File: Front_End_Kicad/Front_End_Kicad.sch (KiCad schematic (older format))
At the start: 41 parts, among them J101 Barrel_Jack, SW101 SW_DIP_x02, SW102 SW_DIP_x02, SW103 SW_DIP_x05, SW104 SW_DIP_x05, U101 LMH6551MM

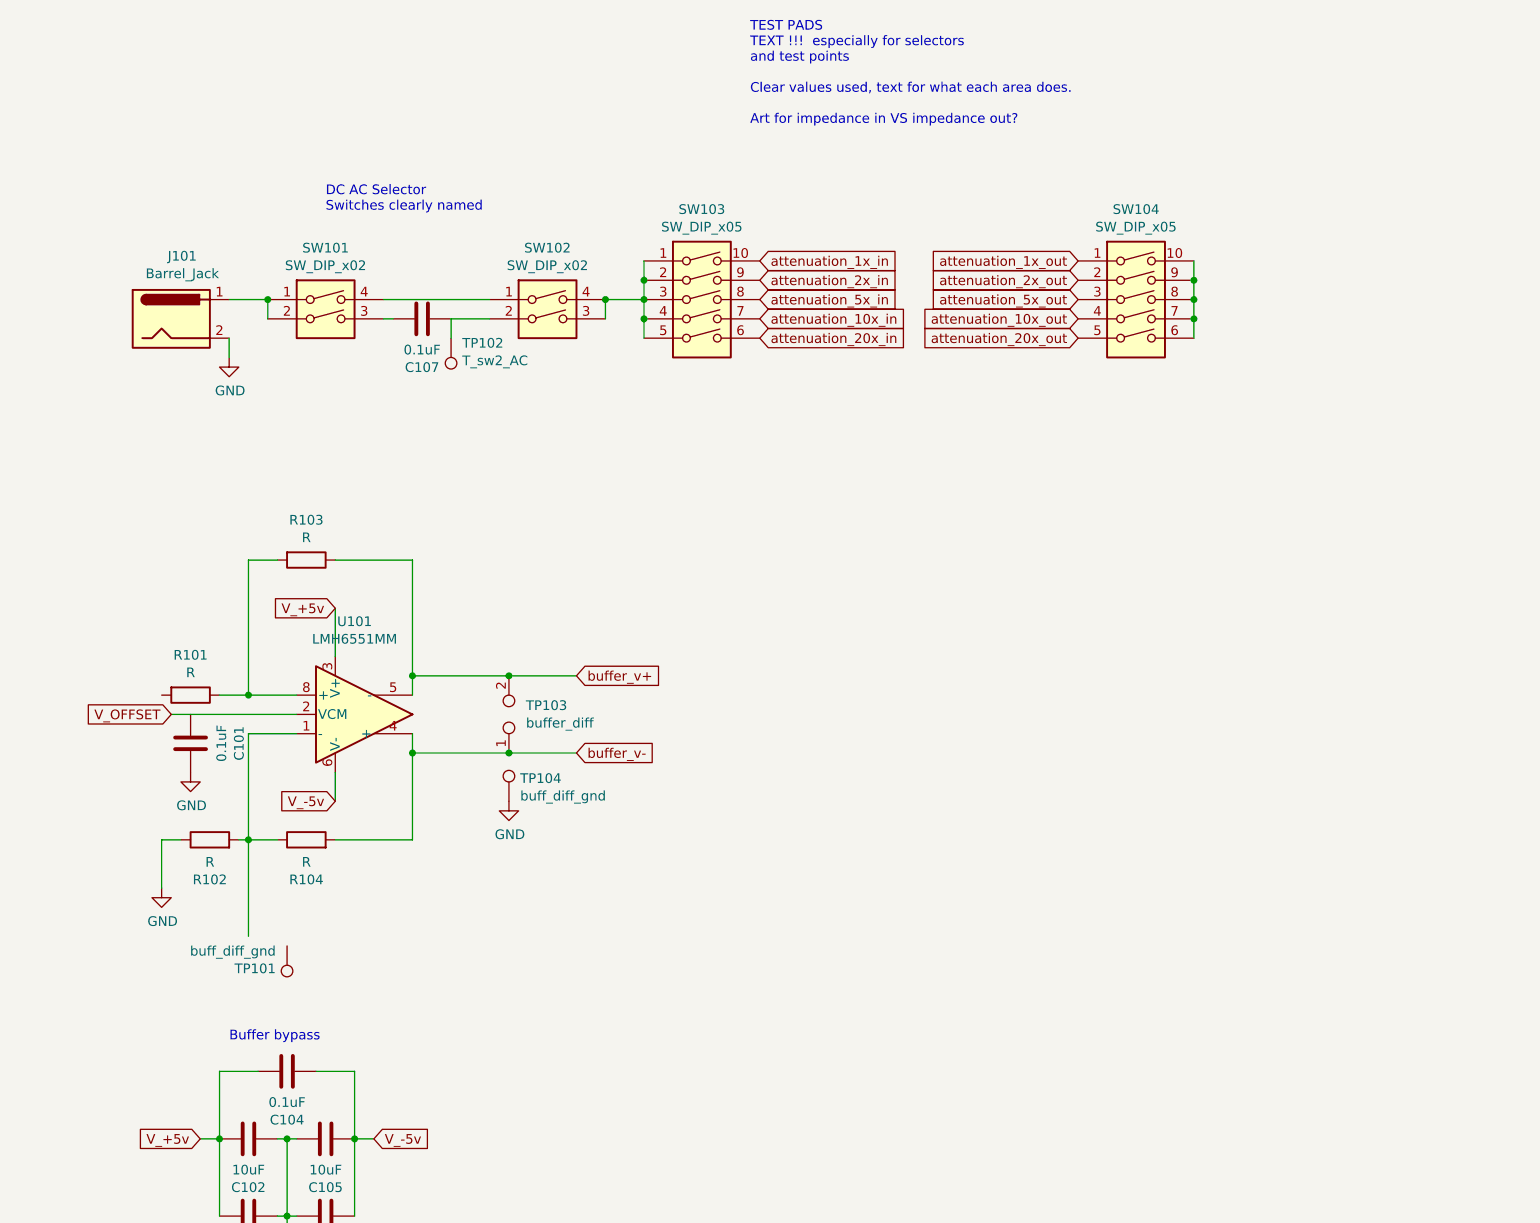
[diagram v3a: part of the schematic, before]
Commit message: All parts designed in schematic and preparing to enter PCB design
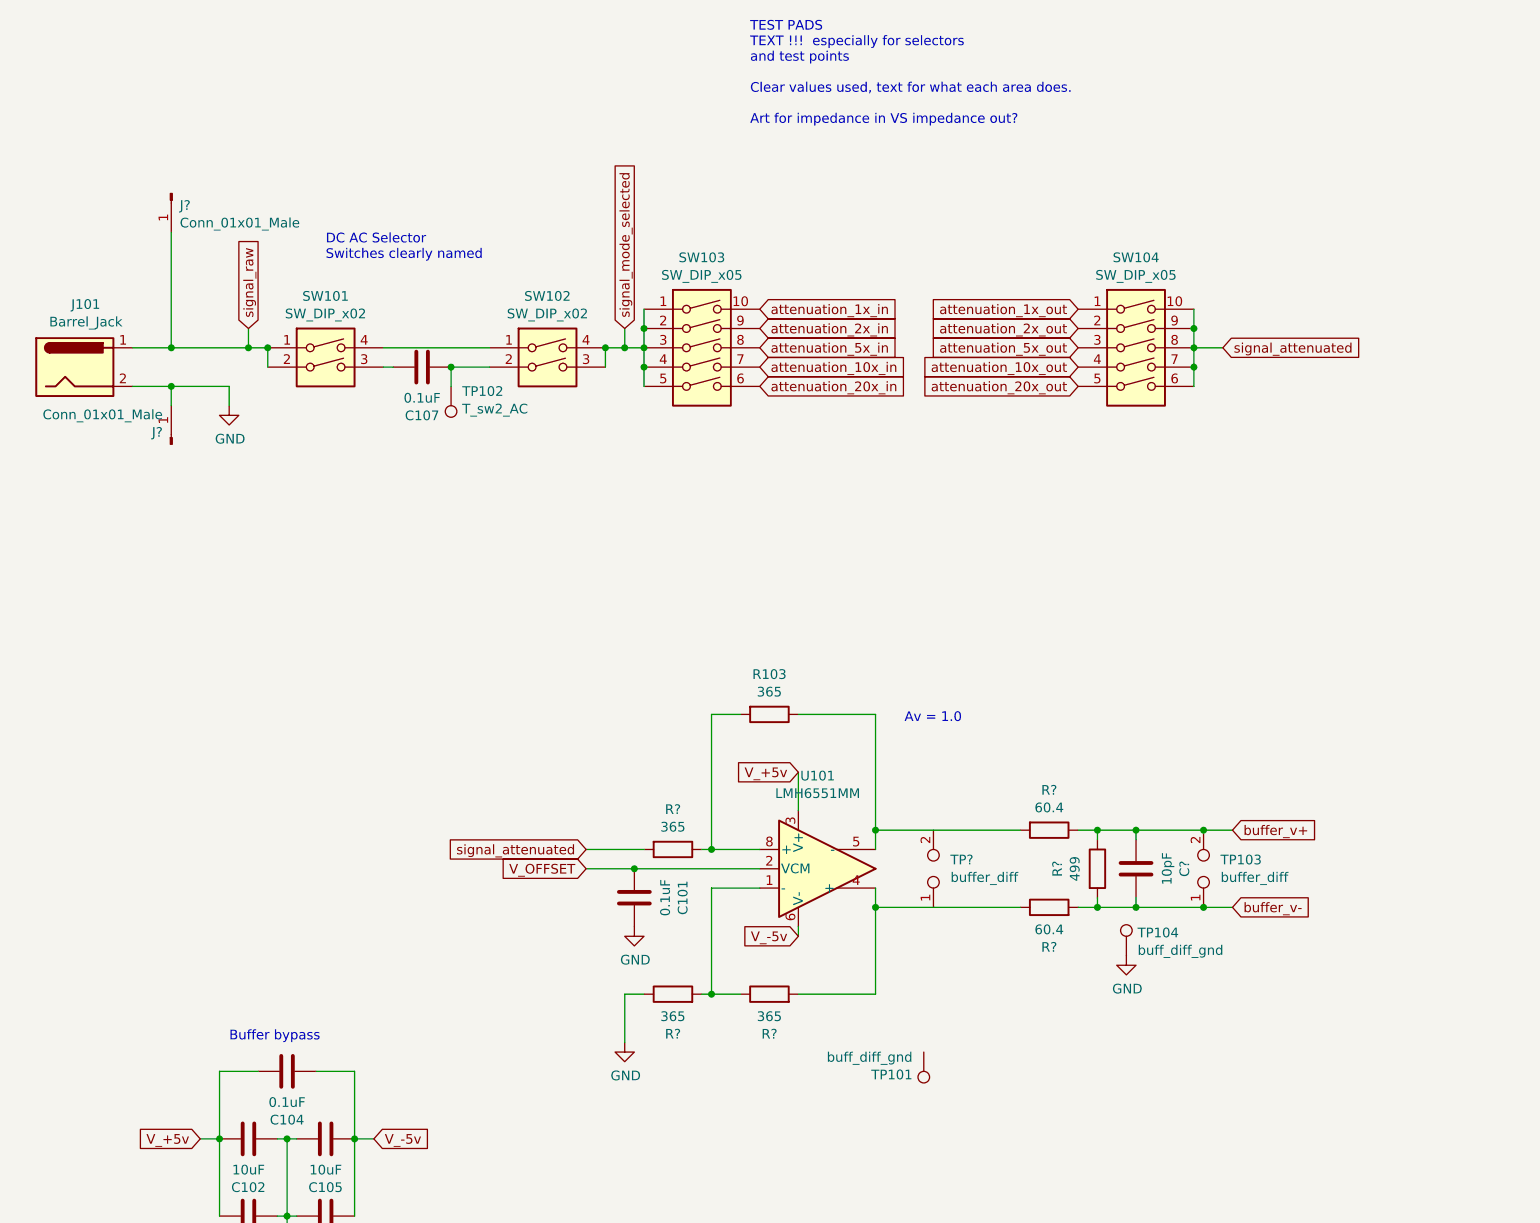
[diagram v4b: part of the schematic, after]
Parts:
- removed R101, R102, R104: R, Resistor_SMD:R_1206_3216Metric, symbol Device:R
- added C?: 10pF, Capacitor_SMD:C_1206_3216Metric, symbol Device:C
- added J? (x2): Conn_01x01_Male, Connector_PinHeader_2.00mm:PinHeader_1x01_P2.00mm_Vertical, symbol Connector:Conn_01x01_Male
- added R? (x3): 365, Resistor_SMD:R_1206_3216Metric, symbol Device:R
- added R? (x2): 60.4, Resistor_SMD:R_1206_3216Metric, symbol Device:R
- added R?: 499, Resistor_SMD:R_1206_3216Metric, symbol Device:R
- added TP?: buffer_diff, TestPoint:TestPoint_2Pads_Pitch5.08mm_Drill1.3mm, symbol Connector:TestPoint_2Pole
- R103: value R -> 365; part_url (none) -> https://www.digikey.com/en/products/detail/yageo/RC1206FR-0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
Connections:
- net GND: now also J?.1 (Pin_1), R?.1
- net V_OFFSET: now also C101.1
- net buffer_v+: now also C?.1, R?.1, R?.1; no longer R103.1, U101.5 (-)
- net buffer_v-: now also C?.2, R?.2, R?.2; no longer U101.4 (+)
- net signal_raw: now reaches J101.1, SW101.1, SW101.2
- net signal_raw: now also J?.1 (Pin_1)
- net signal_mode_selected: now reaches SW102.3, SW102.4, SW103.1, SW103.2, SW103.3, SW103.4, SW103.5
- net signal_attenuated: now reaches SW104.10, SW104.6, SW104.7, SW104.8, SW104.9
- net signal_attenuated: now also R?.2
- net at U101.1 (-): now also R?.1, R?.2
- net at R103.2, U101.8 (+): now also R?.1
- new net: R?.1, R?.2, U101.4 (+)
- new net: R103.1, R?.2, U101.5 (-)
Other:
- note added: "Av = 1.0"
- moved on the sheet: C101, C107, J101, R103, SW101, SW102, SW103, SW104, TP101, TP102, TP103, TP104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

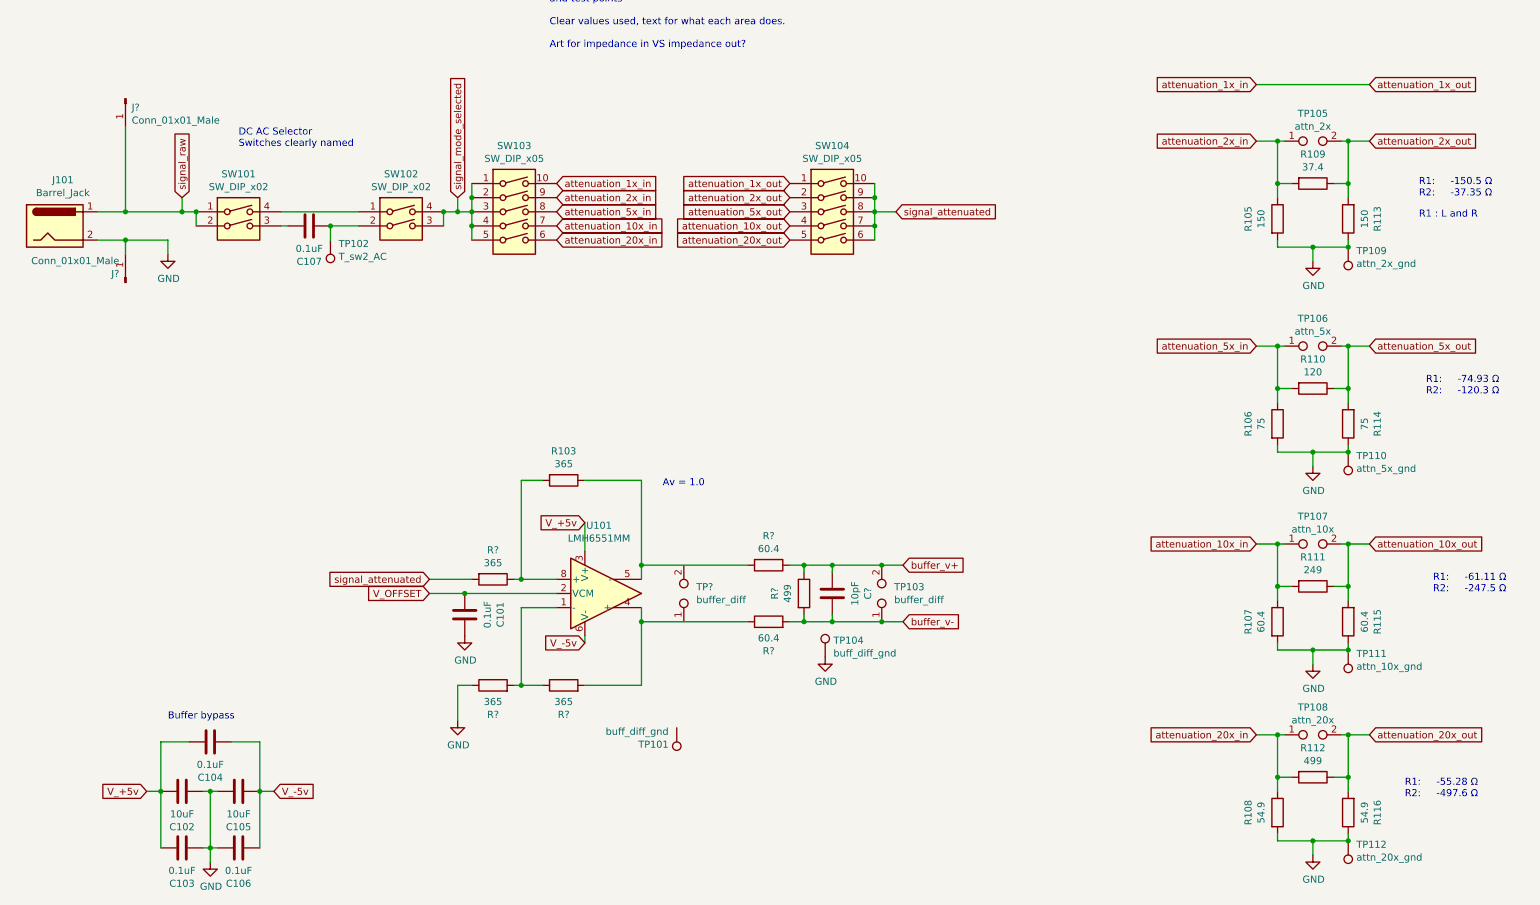
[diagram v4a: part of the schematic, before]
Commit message: Started work on PCB.  Sections seperated and partially connected.  Planning 4 layer
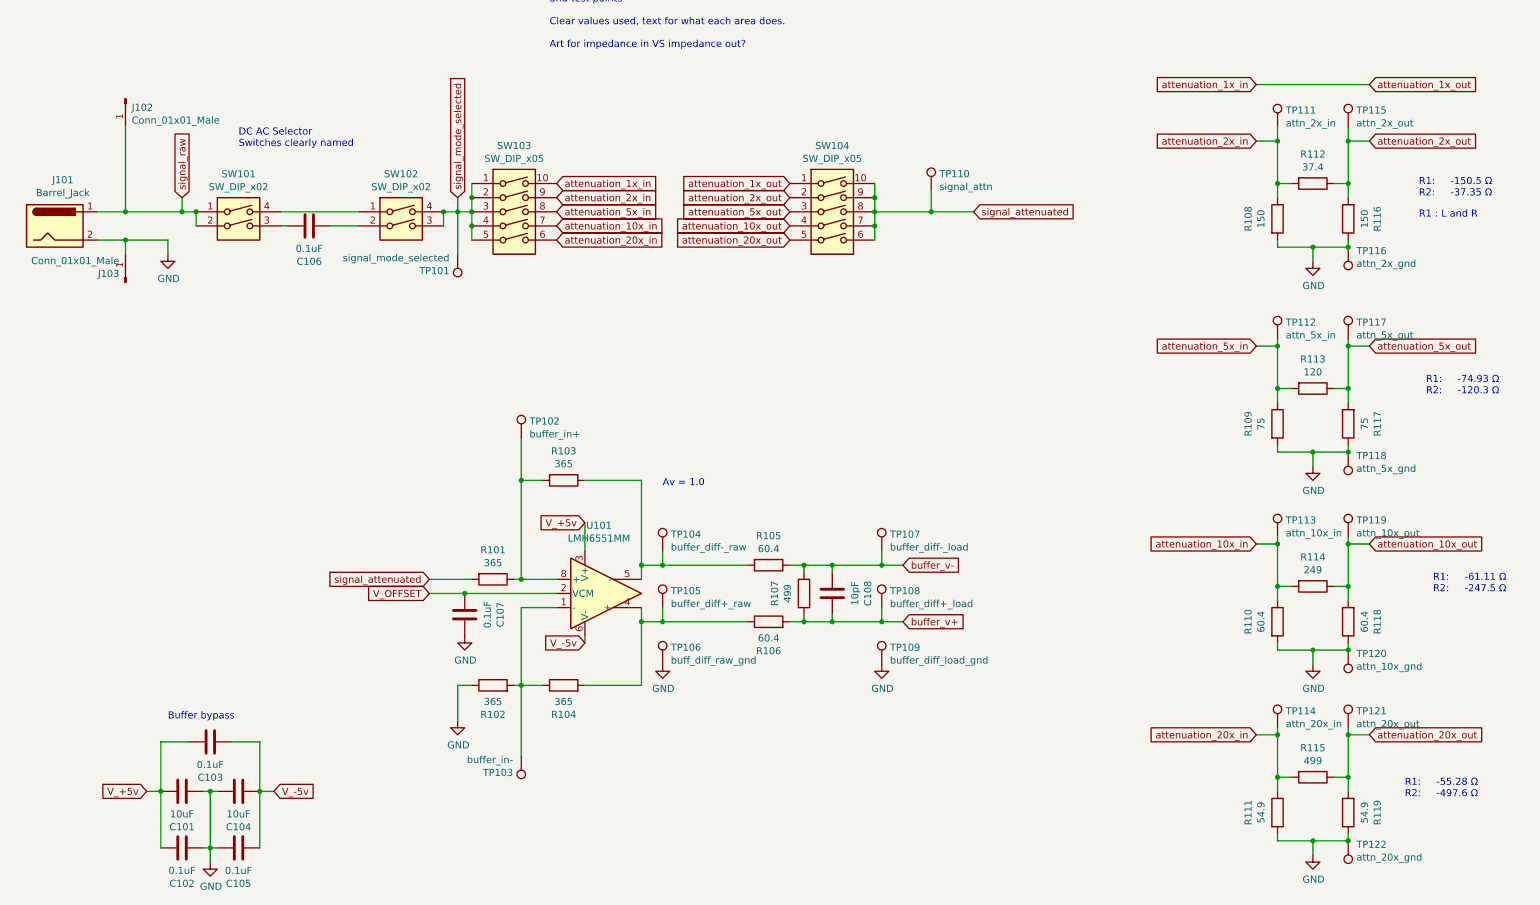
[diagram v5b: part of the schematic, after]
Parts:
- removed TP103, TP?: buffer_diff, TestPoint:TestPoint_2Pads_Pitch5.08mm_Drill1.3mm, symbol Connector:TestPoint_2Pole
- removed TP105: attn_2x, TestPoint:TestPoint_2Pads_Pitch5.08mm_Drill1.3mm, symbol Connector:TestPoint_2Pole
- removed TP106: attn_5x, TestPoint:TestPoint_2Pads_Pitch5.08mm_Drill1.3mm, symbol Connector:TestPoint_2Pole
- removed TP107: attn_10x, TestPoint:TestPoint_2Pads_Pitch5.08mm_Drill1.3mm, symbol Connector:TestPoint_2Pole
- removed TP108: attn_20x, TestPoint:TestPoint_2Pads_Pitch5.08mm_Drill1.3mm, symbol Connector:TestPoint_2Pole
- added TP103: buffer_in-, TestPoint:TestPoint_THTPad_D1.5mm_Drill0.7mm, symbol Connector:TestPoint
- added TP104: buffer_diff-_raw, TestPoint:TestPoint_THTPad_D1.5mm_Drill0.7mm, symbol Connector:TestPoint
- added TP105: buffer_diff+_raw, TestPoint:TestPoint_THTPad_D1.5mm_Drill0.7mm, symbol Connector:TestPoint
- added TP106: buff_diff_raw_gnd, TestPoint:TestPoint_THTPad_1.5x1.5mm_Drill0.7mm, symbol Connector:TestPoint
- added TP107: buffer_diff-_load, TestPoint:TestPoint_THTPad_D1.5mm_Drill0.7mm, symbol Connector:TestPoint
- added TP108: buffer_diff+_load, TestPoint:TestPoint_THTPad_D1.5mm_Drill0.7mm, symbol Connector:TestPoint
- added TP110: signal_attn, TestPoint:TestPoint_THTPad_D1.5mm_Drill0.7mm, symbol Connector:TestPoint
- added TP111: attn_2x_in, TestPoint:TestPoint_THTPad_D1.5mm_Drill0.7mm, symbol Connector:TestPoint
- added TP112: attn_5x_in, TestPoint:TestPoint_THTPad_D1.5mm_Drill0.7mm, symbol Connector:TestPoint
- added TP113: attn_10x_in, TestPoint:TestPoint_THTPad_D1.5mm_Drill0.7mm, symbol Connector:TestPoint
- added TP114: attn_20x_in, TestPoint:TestPoint_THTPad_D1.5mm_Drill0.7mm, symbol Connector:TestPoint
- added TP115: attn_2x_out, TestPoint:TestPoint_THTPad_D1.5mm_Drill0.7mm, symbol Connector:TestPoint
- added TP117: attn_5x_out, TestPoint:TestPoint_THTPad_D1.5mm_Drill0.7mm, symbol Connector:TestPoint
- added TP119: attn_10x_out, TestPoint:TestPoint_THTPad_D1.5mm_Drill0.7mm, symbol Connector:TestPoint
- added TP121: attn_20x_out, TestPoint:TestPoint_THTPad_D1.5mm_Drill0.7mm, symbol Connector:TestPoint
- TP101: value buff_diff_gnd -> signal_mode_selected; footprint TestPoint:TestPoint_THTPad_3.0x3.0mm_Drill1.5mm -> TestPoint:TestPoint_THTPad_D1.5mm_Drill0.7mm
- TP102: value T_sw2_AC -> buffer_in+; footprint TestPoint:TestPoint_THTPad_3.0x3.0mm_Drill1.5mm -> TestPoint:TestPoint_THTPad_D1.5mm_Drill0.7mm
- TP109: renamed from TP104; value buff_diff_gnd -> buffer_diff_load_gnd; footprint TestPoint:TestPoint_THTPad_3.0x3.0mm_Drill1.5mm -> TestPoint:TestPoint_THTPad_1.5x1.5mm_Drill0.7mm
- TP118: renamed from TP110; footprint TestPoint:TestPoint_THTPad_3.0x3.0mm_Drill1.5mm -> TestPoint:TestPoint_THTPad_1.5x1.5mm_Drill0.7mm
- TP120: renamed from TP111; footprint TestPoint:TestPoint_THTPad_3.0x3.0mm_Drill1.5mm -> TestPoint:TestPoint_THTPad_1.5x1.5mm_Drill0.7mm
- TP122: renamed from TP112; footprint TestPoint:TestPoint_THTPad_3.0x3.0mm_Drill1.5mm -> TestPoint:TestPoint_THTPad_1.5x1.5mm_Drill0.7mm
- gave numbers to parts that had none: 9
- renumbered C102 to C101, C103 to C102, C104 to C103, C105 to C104, C106 to C105, C107 to C106, C101 to C107, R105 to R108, R106 to R109, R107 to R110, R108 to R111, R109 to R112, R110 to R113, R111 to R114, R112 to R115, R113 to R116, R114 to R117, R115 to R118, R116 to R119, TP109 to TP116
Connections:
- net GND: now also TP106.1
- net attenuation_10x_in: now also TP113.1
- net attenuation_10x_out: now also TP119.1
- net attenuation_20x_in: now also TP114.1
- net attenuation_20x_out: now also TP121.1
- net attenuation_2x_in: now also TP111.1
- net attenuation_2x_out: now also TP115.1
- net attenuation_5x_in: now also TP112.1
- net attenuation_5x_out: now also TP117.1
- net buffer_v+: now also C108.2, R106.2, R107.2, TP108.1; no longer C108.1, R105.1, R107.1
- net buffer_v-: now also C108.1, R105.1, R107.1, TP107.1; no longer C108.2, R106.2, R107.2
- net signal_attenuated: now also TP110.1
- net signal_mode_selected: now also TP101.1
- net at C106.1, SW102.2: no longer TP102.1
- net at R102.2, R104.1, U101.1 (-): now also TP103.1
- net at R104.2, R106.1, U101.4 (+): now also TP105.1
- net at R103.1, R105.2, U101.5 (-): now also TP104.1
- net at R101.1, R103.2, U101.8 (+): now also TP102.1
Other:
- moved on the sheet: TP109
